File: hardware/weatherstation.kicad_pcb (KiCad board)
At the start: 2 copper layers, 53.3 x 53.3 mm, 30 parts, among them J1 Conn_02x13_Odd_Even, J10 Conn_01x03_Male, J2 Conn_01x02_Male, J3 Conn_01x02_Male, J4 Conn_01x02_Male, J5 Conn_01x02_Male, J6 Conn_01x02_Male, J7 Conn_01x02_Male, J8 Conn_01x02_Male, J9 Conn_01x02_Male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

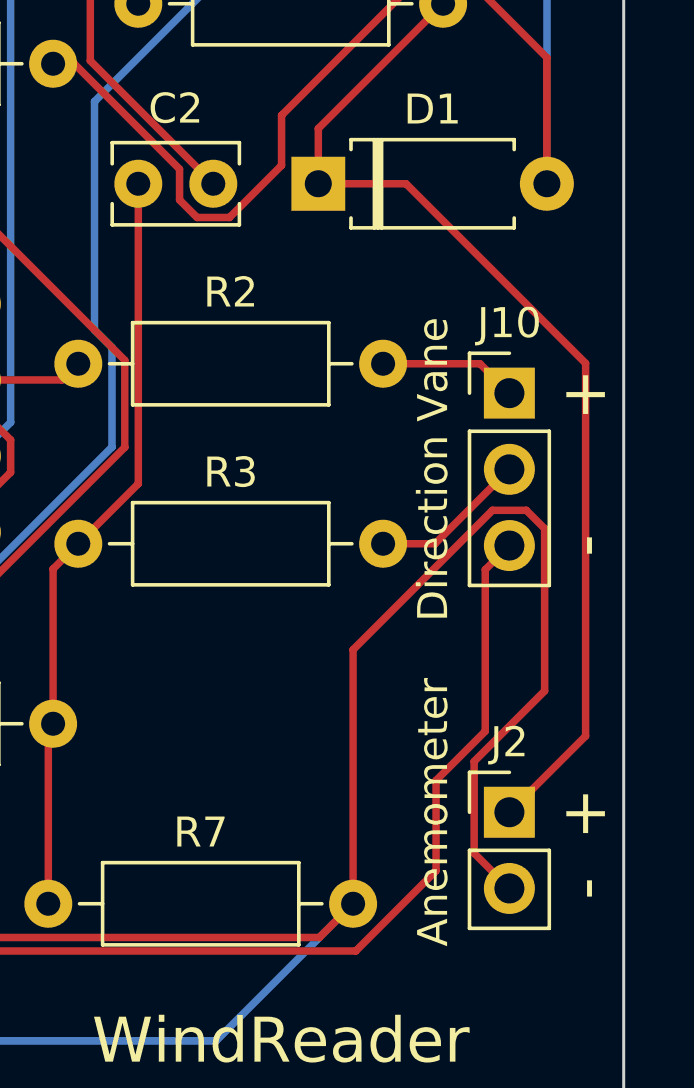
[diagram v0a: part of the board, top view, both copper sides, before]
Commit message: Fixed ground of anemometer going ground problem
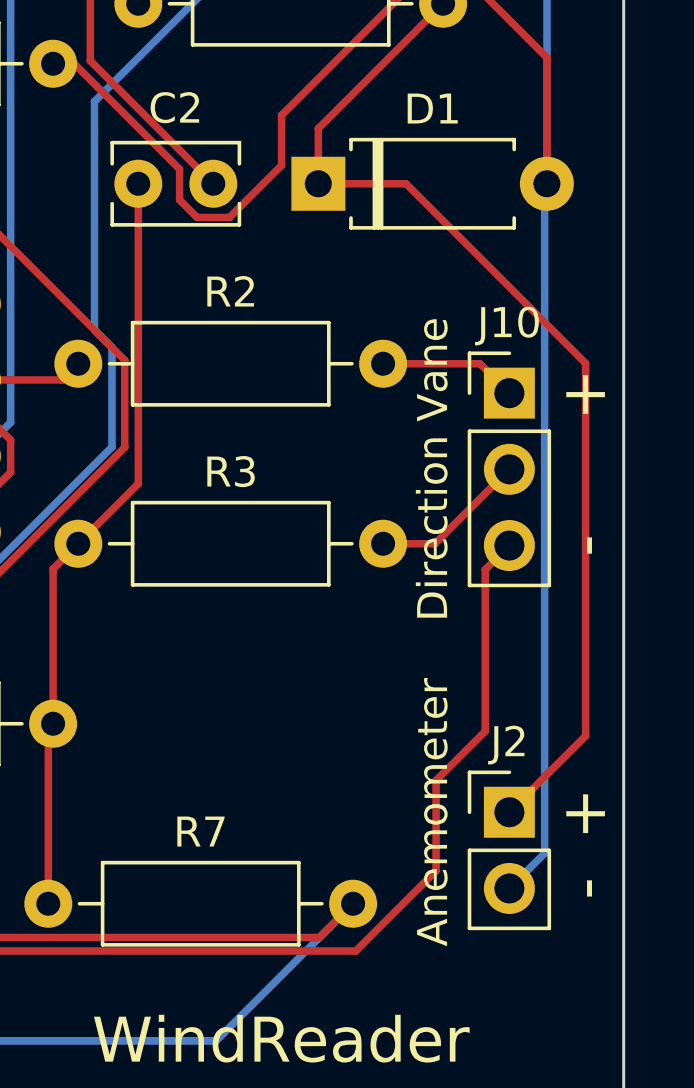
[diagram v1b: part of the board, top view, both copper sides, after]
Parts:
- R10: value R -> 330
- R5, R6: value R -> 100k
- R8: value R -> 1k
- R9: value R -> 10k
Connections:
- J2 pad 2: GND -> Net-(C1-Pad2)
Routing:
- net GND: track 275.5 -> 243.9 mm
- net Net-(C1-Pad2): track 106.5 -> 131.7 mm
